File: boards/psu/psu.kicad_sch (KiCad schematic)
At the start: 10 parts, among them IC1 NSD10-12D12, J3 Conn_01x03

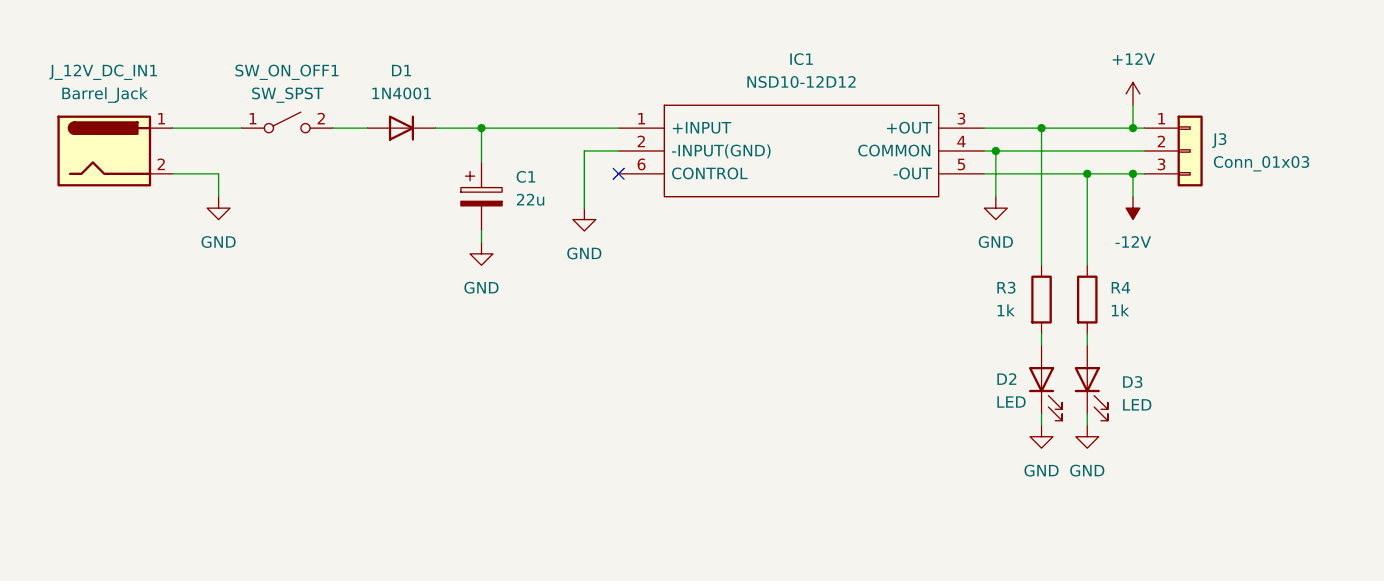
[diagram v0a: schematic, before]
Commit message: Created PSU board
https://github.com/shmoergh/hog/issues/4
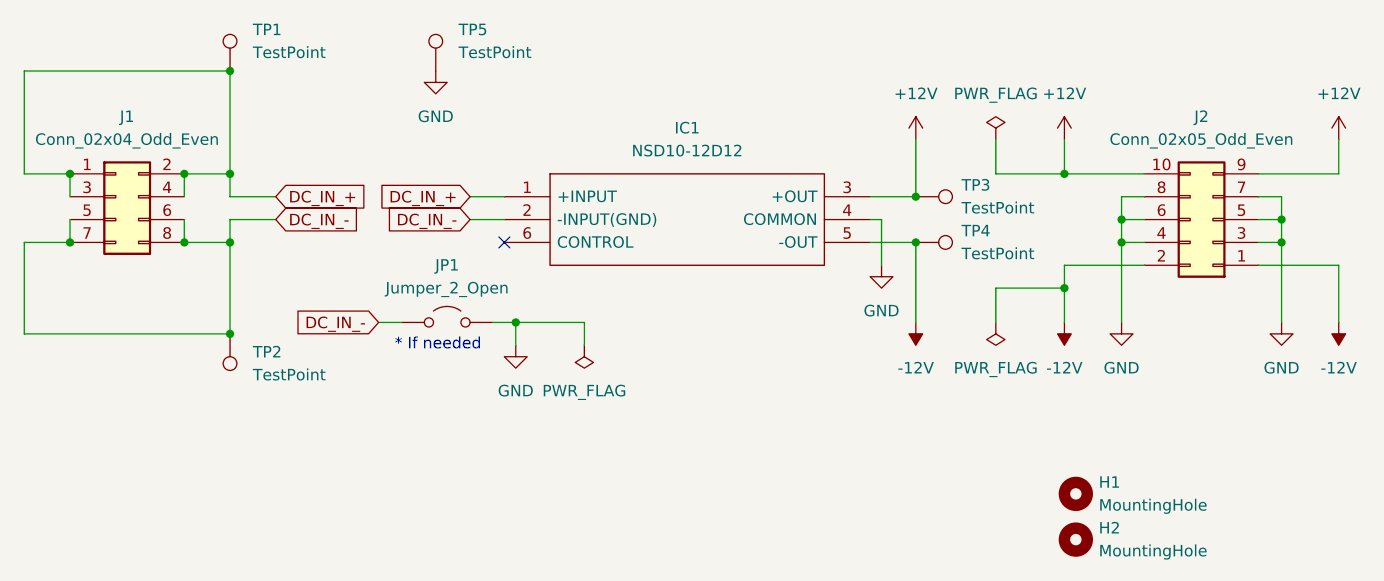
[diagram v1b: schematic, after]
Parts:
- removed C1: 22u, symbol Device:C_Polarized
- removed D1: 1N4001, Diode_THT:D_DO-41_SOD81_P10.16mm_Horizontal, symbol Diode:1N4001
- removed D2, D3: LED, symbol Device:LED
- removed J3: Conn_01x03, symbol Connector_Generic:Conn_01x03
- removed J_12V_DC_IN1: Barrel_Jack, symbol Connector:Barrel_Jack
- removed R3, R4: 1k, symbol Device:R
- removed SW_ON_OFF1: SW_SPST, symbol Switch:SW_SPST
- added H1, H2: MountingHole, MountingHole:MountingHole_3mm_Pad, symbol Mechanical:MountingHole
- added J1: Conn_02x04_Odd_Even, Connector_PinSocket_2.54mm:PinSocket_2x04_P2.54mm_Vertical, symbol Connector_Generic:Conn_02x04_Odd_Even
- added J2: Conn_02x05_Odd_Even, Connector_PinSocket_2.54mm:PinSocket_2x05_P2.54mm_Vertical, symbol Connector_Generic:Conn_02x05_Odd_Even
- added JP1: Jumper_2_Open, Jumper:SolderJumper-2_P1.3mm_Open_Pad1.0x1.5mm, symbol Jumper:Jumper_2_Open
- added TP1, TP2, TP3, TP4, TP5: TestPoint, TestPoint:TestPoint_THTPad_2.0x2.0mm_Drill1.0mm, symbol Connector:TestPoint
- IC1: Description_1 (none) -> Isolated DC/DC Converters 12Vin 5V1A -5V1A 10W
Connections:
- net +12V: now also J2.10 (Pin_10), J2.9 (Pin_9), TP3.1
- net -12V: now also J2.1 (Pin_1), J2.2 (Pin_2), TP4.1
- net GND: now also J2.3 (Pin_3), J2.4 (Pin_4), J2.5 (Pin_5), J2.6 (Pin_6), J2.7 (Pin_7), J2.8 (Pin_8), JP1.2 (B), TP5.1; no longer IC1.2 (-INPUT(GND))
- net DC_IN_+: now reaches IC1.1 (+INPUT)
- net DC_IN_+: now also J1.1 (Pin_1), J1.2 (Pin_2), J1.3 (Pin_3), J1.4 (Pin_4), TP1.1
- new net DC_IN_-: IC1.2 (-INPUT(GND)), J1.5 (Pin_5), J1.6 (Pin_6), J1.7 (Pin_7), J1.8 (Pin_8), JP1.1 (A), TP2.1
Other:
- note added: "* If needed"
- moved on the sheet: IC1

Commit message: Created BOM for PSU board
ref https://github.com/shmoergh/hog/issues/19
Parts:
- H1, H2: Part No. (none) -> N/A; Part URL (none) -> N/A; Vendor (none) -> N/A
- IC1: Description_1 Isolated DC/DC Converters 12Vin 5V1A -5V1A 10W -> (none); Manufacturer_Part_Number NSD10-12D5 -> NSD10-12D12; Mouser Price/Stock https://www.mouser.co.uk/ProductDetail/MEAN-WELL/NSD10-12D5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 -> (none); Part No. (none) -> 709-NSD10-12D12; Part URL (none) -> https://mou.sr/3ZpECrS; Vendor (none) -> Mouser
- J1: Part No. (none) -> 737-RS2-08-G; Part URL (none) -> https://mou.sr/41qYCwK; Vendor (none) -> Mouser
- J2: Part No. (none) -> 737-RS2-10-G; Part URL (none) -> https://mou.sr/3ZuUKrQ; Vendor (none) -> Mouser
- JP1, TP1, TP2, TP3, TP4, TP5: Part No. (none) -> N/A; Part URL (none) -> N/A; Vendor (none) -> N/A; now left out of the parts list
